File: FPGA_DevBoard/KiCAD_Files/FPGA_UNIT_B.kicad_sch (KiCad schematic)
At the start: 67 parts, among them J15 6130XX11121_61301611121, J16 6130XX11121_61301611121, J7 L77HDE15SD1CH4F, U19 XC7S50-1FTGB196C, U24 USBLC6-2SC6, U25 USBLC6-2SC6, U26 USBLC6-2SC6, U27 USBLC6-2SC6, U28 USBLC6-2SC6, U29 USBLC6-2SC6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

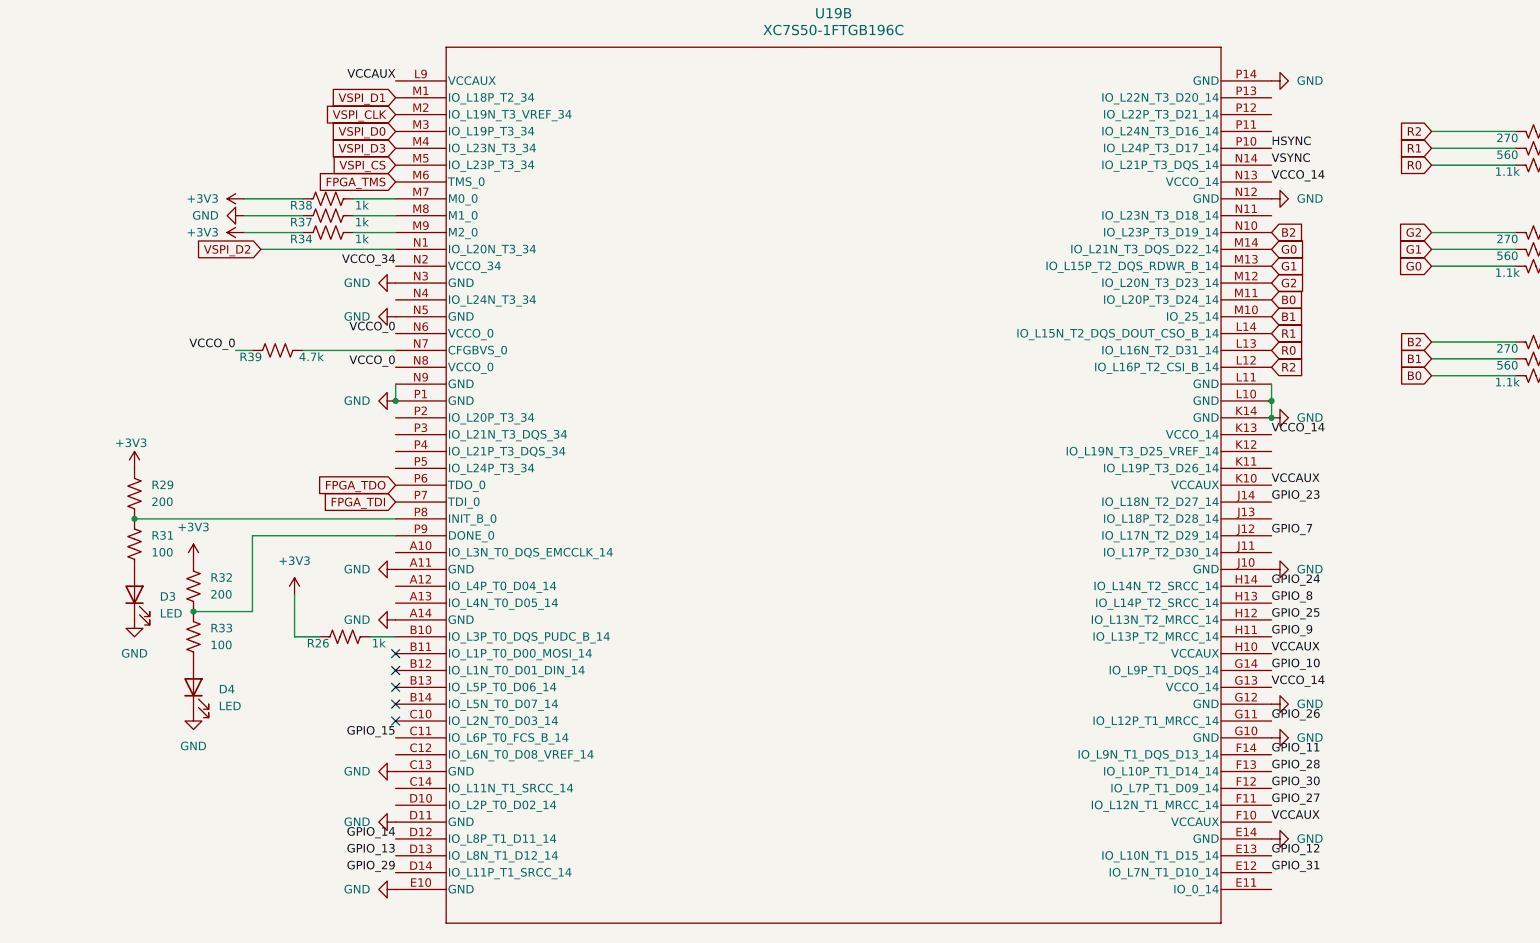
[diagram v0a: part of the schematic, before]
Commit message: ESD
Added ESD to the main USB programmer. Also added terminating resistors and test points. Also updated some planes to make sure everything was connected.
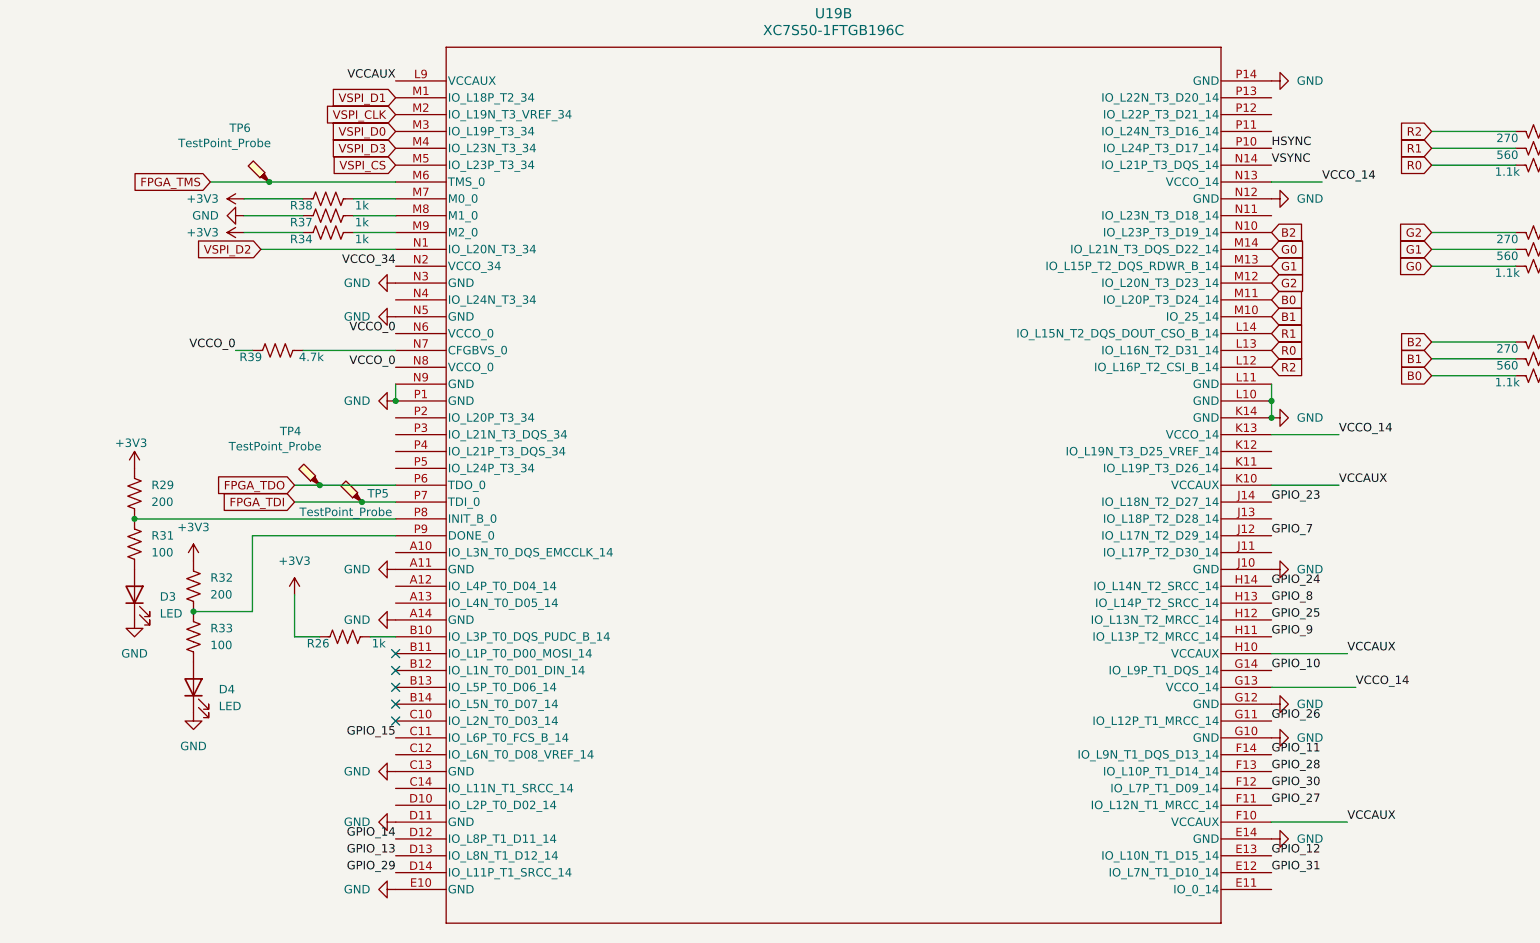
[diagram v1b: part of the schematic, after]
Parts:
- added TP4, TP5, TP6: TestPoint_Probe, TestPoint:TestPoint_Pad_D1.0mm, symbol Connector:TestPoint_Probe
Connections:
- net FPGA_TDI: now also TP5.1
- net FPGA_TDO: now also TP4.1
- net FPGA_TMS: now also TP6.1

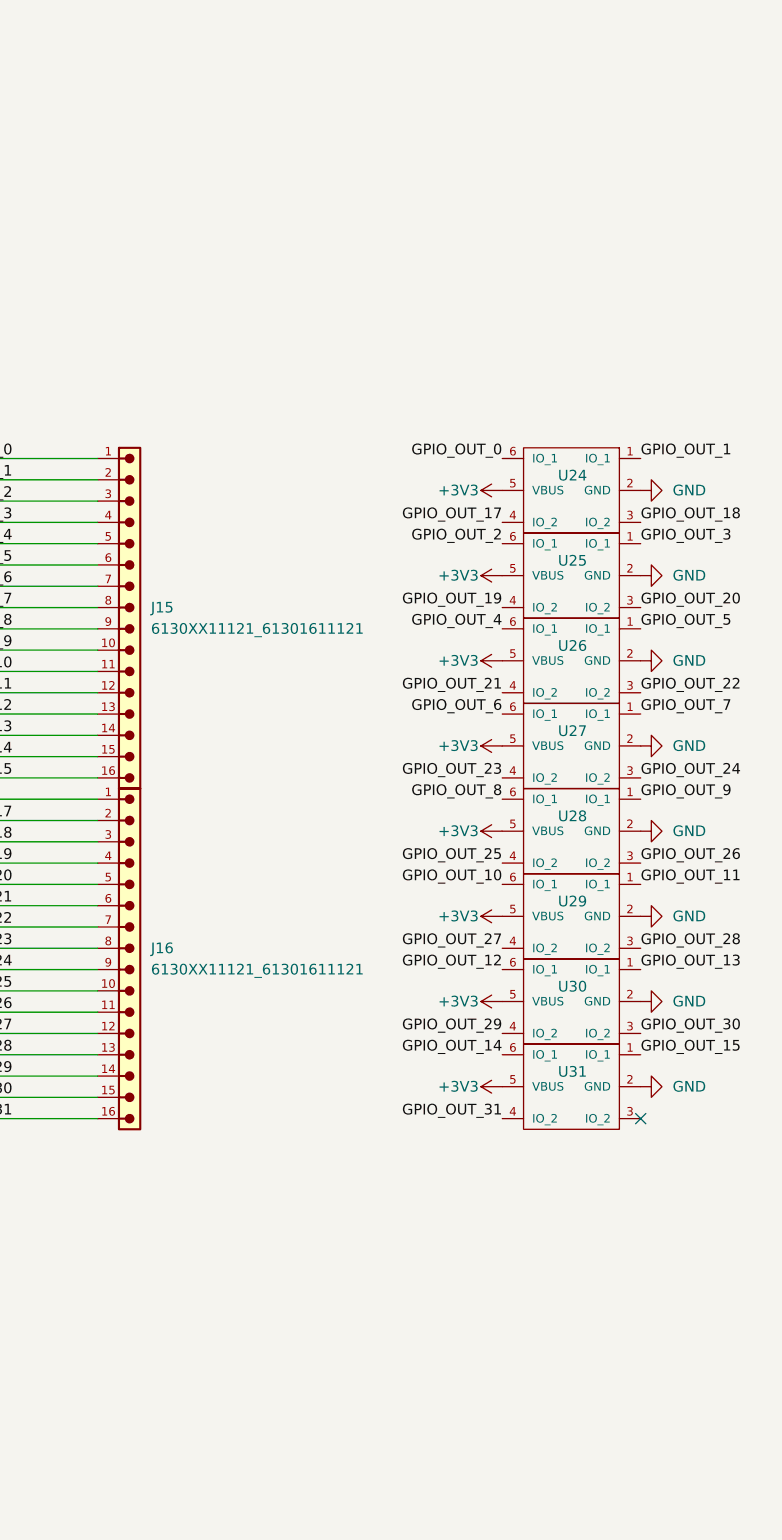
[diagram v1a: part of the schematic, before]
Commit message: Updated ESD for both the USB hub outputs and GPIO output
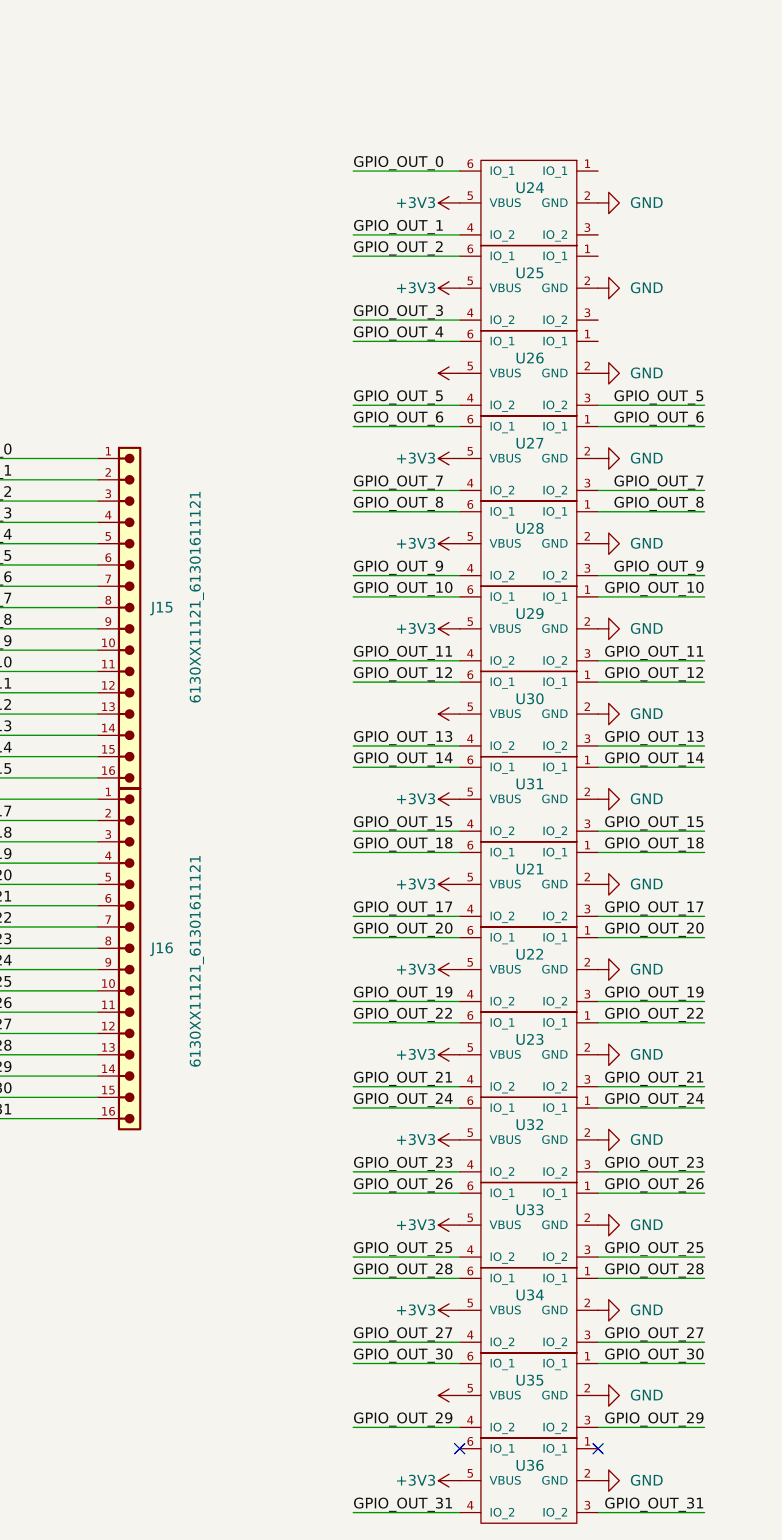
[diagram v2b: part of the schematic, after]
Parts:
- added U21, U22, U23, U32, U33, U34, U35, U36: USBLC6-2SC6, USB_HUB:SOT95P280X145-6N, symbol Test:USBLC6-2SC6
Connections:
- net +3V3: now also U21.5 (VBUS), U22.5 (VBUS), U23.5 (VBUS), U32.5 (VBUS), U33.5 (VBUS), U34.5 (VBUS), U35.5 (VBUS), U36.5 (VBUS)
- net GND: now also U21.2 (GND), U22.2 (GND), U23.2 (GND), U32.2 (GND), U33.2 (GND), U34.2 (GND), U35.2 (GND), U36.2 (GND)
- net GPIO_OUT_1: now also U24.4 (IO_2); no longer U24.1 (IO_1)
- net GPIO_OUT_10: now also U29.1 (IO_1)
- net GPIO_OUT_11: now also U29.3 (IO_2), U29.4 (IO_2); no longer U29.1 (IO_1)
- net GPIO_OUT_12: now also U30.1 (IO_1)
- net GPIO_OUT_13: now also U30.3 (IO_2), U30.4 (IO_2); no longer U30.1 (IO_1)
- net GPIO_OUT_14: now also U31.1 (IO_1)
- net GPIO_OUT_15: now also U31.3 (IO_2), U31.4 (IO_2); no longer U31.1 (IO_1)
- net GPIO_OUT_17: now also U21.3 (IO_2), U21.4 (IO_2); no longer U24.4 (IO_2)
- net GPIO_OUT_18: now also U21.1 (IO_1), U21.6 (IO_1); no longer U24.3 (IO_2)
- net GPIO_OUT_19: now also U22.3 (IO_2), U22.4 (IO_2); no longer U25.4 (IO_2)
- net GPIO_OUT_20: now also U22.1 (IO_1), U22.6 (IO_1); no longer U25.3 (IO_2)
- net GPIO_OUT_21: now also U23.3 (IO_2), U23.4 (IO_2); no longer U26.4 (IO_2)
- net GPIO_OUT_22: now also U23.1 (IO_1), U23.6 (IO_1); no longer U26.3 (IO_2)
- net GPIO_OUT_23: now also U32.3 (IO_2), U32.4 (IO_2); no longer U27.4 (IO_2)
- net GPIO_OUT_24: now also U32.1 (IO_1), U32.6 (IO_1); no longer U27.3 (IO_2)
- net GPIO_OUT_25: now also U33.3 (IO_2), U33.4 (IO_2); no longer U28.4 (IO_2)
- net GPIO_OUT_26: now also U33.1 (IO_1), U33.6 (IO_1); no longer U28.3 (IO_2)
- net GPIO_OUT_27: now also U34.3 (IO_2), U34.4 (IO_2); no longer U29.4 (IO_2)
- net GPIO_OUT_28: now also U34.1 (IO_1), U34.6 (IO_1); no longer U29.3 (IO_2)
- net GPIO_OUT_29: now also U35.3 (IO_2), U35.4 (IO_2); no longer U30.4 (IO_2)
- net GPIO_OUT_3: now also U25.4 (IO_2); no longer U25.1 (IO_1)
- net GPIO_OUT_30: now also U35.1 (IO_1), U35.6 (IO_1); no longer U30.3 (IO_2)
- net GPIO_OUT_31: now also U36.3 (IO_2), U36.4 (IO_2); no longer U31.4 (IO_2)
- net GPIO_OUT_5: now also U26.3 (IO_2), U26.4 (IO_2); no longer U26.1 (IO_1)
- net GPIO_OUT_6: now also U27.1 (IO_1)
- net GPIO_OUT_7: now also U27.3 (IO_2), U27.4 (IO_2); no longer U27.1 (IO_1)
- net GPIO_OUT_8: now also U28.1 (IO_1)
- net GPIO_OUT_9: now also U28.3 (IO_2), U28.4 (IO_2); no longer U28.1 (IO_1)
- no-connect marks 11 -> 12
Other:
- moved on the sheet: U24, U25, U26, U27, U28, U29, U30, U31

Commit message: forgot to save schematic when pushing last commit
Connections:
- net GPIO_OUT_0: now also U24.1 (IO_1)
- net GPIO_OUT_1: now also U24.3 (IO_2)
- net GPIO_OUT_2: now also U25.1 (IO_1)
- net GPIO_OUT_3: now also U25.3 (IO_2)
- net GPIO_OUT_4: now also U26.1 (IO_1)
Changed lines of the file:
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@@
+	(wire
+		(pts
+			(xy 388.62 92.71) (xy 401.32 92.71)
+		)
+		(stroke
+			(width 0)
+			(type default)
+		)
+	)
 	(wire
 		(pts
@@
 	(wire
 		(pts
+			(xy 388.62 82.55) (xy 401.32 82.55)
+		)
+		(stroke
+			(width 0)
+			(type default)
+		)
+	)
+	(wire
+		(pts
 			(xy 372.11 143.51) (xy 359.41 143.51)
 		)
@@
 	(wire
 		(pts
+			(xy 388.62 95.25) (xy 401.32 95.25)
+		)
+		(stroke
+			(width 0)
+			(type default)
+		)
+	)
+	(wire
+		(pts
 			(xy 64.77 49.53) (xy 83.82 49.53)
 		)
@@
 	(wire
 		(pts
+			(xy 388.62 74.93) (xy 401.32 74.93)
+		)
+		(stroke
+			(width 0)
+			(type default)
+		)
+	)
+	(wire
+		(pts
 			(xy 372.11 173.99) (xy 359.41 173.99)
 		)
@@
 		(pts
 			(xy 240.03 41.91) (xy 252.73 41.91)
+		)
+		(stroke
+			(width 0)
+			(type default)
+		)
+	)
+	(wire
+		(pts
+			(xy 388.62 85.09) (xy 401.32 85.09)
 		)
 		(stroke
@@
 		)
 	)
+	(label "GPIO_OUT_3"
+		(at 401.32 92.71 180)
+		(effects
+			(font
+				(size 1.27 1.27)
+			)
+			(justify right bottom)
+		)
+	)
 	(label "GPIO_OUT_13"
 		(at 359.41 143.51 0)
@@
 		)
 	)
+	(label "GPIO_OUT_2"
+		(at 401.32 85.09 180)
+		(effects
+			(font
+				(size 1.27 1.27)
+			)
+			(justify right bottom)
+		)
+	)
 	(label "GPIO_OUT_18"
 		(at 359.41 156.21 0)
@@
 		)
 	)
+	(label "GPIO_OUT_1"
+		(at 401.32 82.55 180)
+		(effects
+			(font
+				(size 1.27 1.27)
+			)
+			(justify right bottom)
+		)
+	)
 	(label "VCCAUX"
 		(at 226.06 95.25 0)
@@
 		)
 	)
+	(label "GPIO_OUT_4"
+		(at 401.32 95.25 180)
+		(effects
+			(font
+				(size 1.27 1.27)
+			)
+			(justify right bottom)
+		)
+	)
 	(label "GPIO_12"
 		(at 215.9 151.13 0)
@@
 		)
 	)
+	(label "GPIO_OUT_0"
+		(at 401.32 74.93 180)
+		(effects
+			(font
+				(size 1.27 1.27)
+			)
+			(justify right bottom)
+		)
+	)

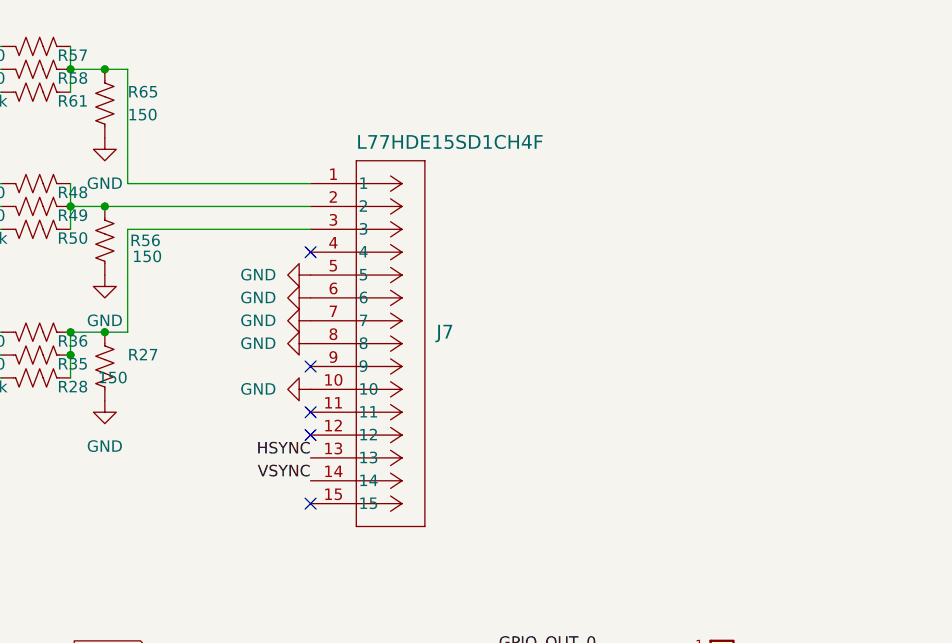
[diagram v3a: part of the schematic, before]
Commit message: added ESD to BGA and length matched it
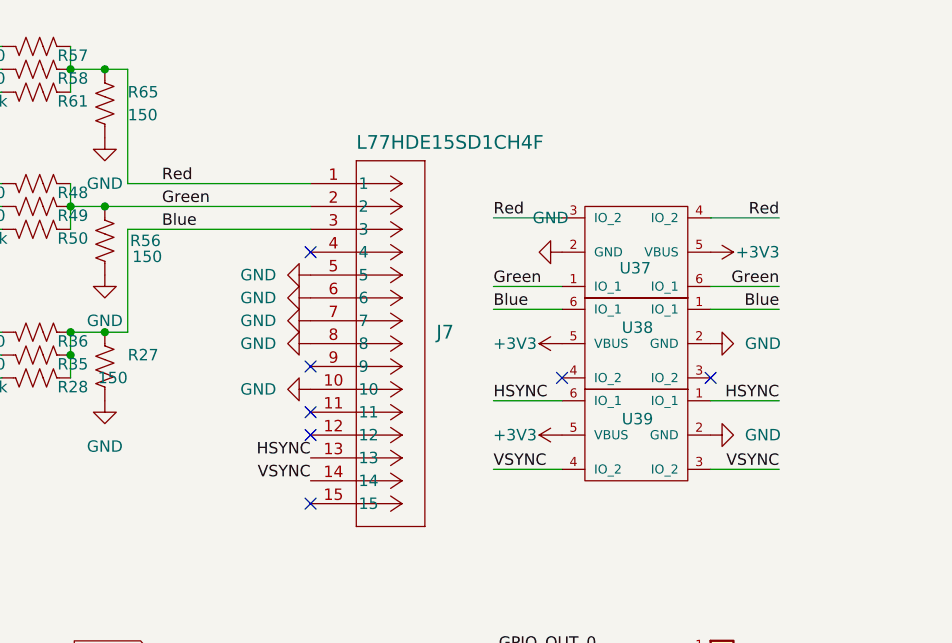
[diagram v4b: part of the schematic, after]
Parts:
- added U37, U38, U39: USBLC6-2SC6, USB_HUB:SOT95P280X145-6N, symbol Test:USBLC6-2SC6
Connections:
- net +3V3: now also U37.5 (VBUS), U38.5 (VBUS), U39.5 (VBUS)
- net GND: now also U37.2 (GND), U38.2 (GND), U39.2 (GND)
- net HSYNC: now also U39.1 (IO_1), U39.6 (IO_1)
- net VSYNC: now also U39.3 (IO_2), U39.4 (IO_2)
- net Red: now reaches J7.1, R57.2, R58.2, R61.2, R65.1
- net Red: now also U37.3 (IO_2), U37.4 (IO_2)
- net Blue: now reaches J7.3, R27.1, R28.2, R35.2, R36.2
- net Blue: now also U38.1 (IO_1), U38.6 (IO_1)
- net Green: now reaches J7.2, R48.2, R49.2, R50.2, R56.1
- net Green: now also U37.1 (IO_1), U37.6 (IO_1)
- no-connect marks 12 -> 14
